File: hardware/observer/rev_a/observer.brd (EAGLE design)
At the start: 44.5 x 44.5 mm, 27 parts, among them J1 CON_HEADER_2X05-PTH+SHROUDED_A, U1 LPS331AP, U2 MPU-9250, U3 SI1147, U4 SI7021, U5 ATUM

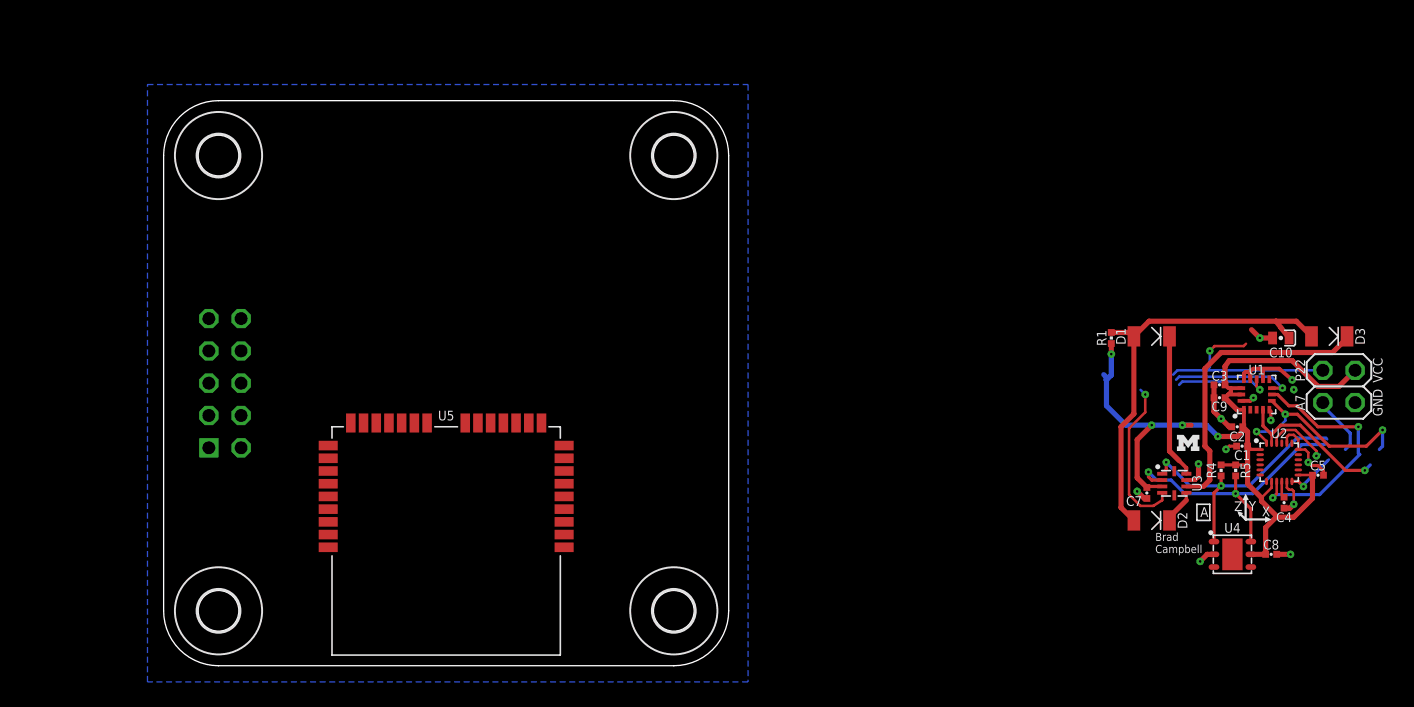
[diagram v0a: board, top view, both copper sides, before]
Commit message: mostly routed
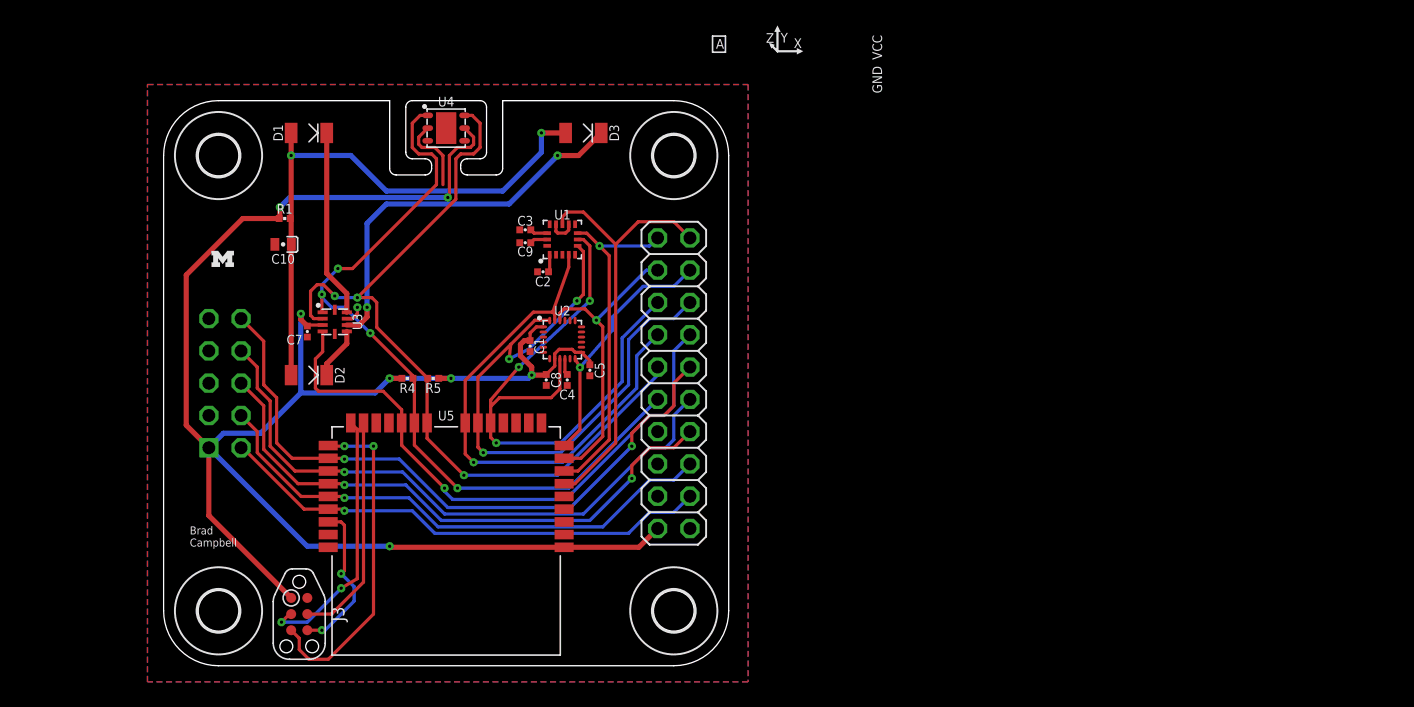
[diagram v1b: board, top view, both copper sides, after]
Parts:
- removed J2: (no value), pinhead:2X02
- added J3: TC2030-CC2538-BL-NL, connector:TC2030-IDC-NL
- added JP1: (no value), pinhead:2X10
- moved C10 78.8 mm to (9.40, 33.1)
- moved LOGO1 77.3 mm to (4.65, 32.0)
- moved U4 70.4 mm to (22.2, 42.3)
- moved D1 68.2 mm to (11.4, 41.9)
- moved D2 67.3 mm to (11.4, 22.9)
- moved C7 67.3 mm to (11.3, 26.3)
- moved U3 67.3 mm to (13.5, 27.1)
- moved R1 65.7 mm to (9.53, 35.2), turned to 180 degrees
- moved R4 64.4 mm to (19.2, 22.6), turned to 180 degrees
- moved R5 63.5 mm to (21.2, 22.6), turned to 0 degrees
- moved D3 60.8 mm to (33.0, 41.9)
- moved C8 58.6 mm to (30.1, 22.5), turned to 270 degrees
- moved C5 57.9 mm to (33.5, 23.2), turned to 270 degrees
- moved C4 57.2 mm to (31.8, 22.5)
- moved U2 57.2 mm to (31.4, 25.7)
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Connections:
- removed net 3V3: J1.1
- removed net A7: J2.2
- removed net MOTOR_CTRL: J2.4
- new net !RESET: J3.6, U5.30
- new net AA: JP1.13
- new net BB: JP1.15
- new net BTLDR_CTRL: J3.5, U5.24
- new net BTLDR_RX: J3.4, U5.22
- new net BTLDR_TX: J3.3, U5.23
- new net CC: JP1.17
- new net UNUSED: U5.21
- new net UNUSED2: U5.20
- net !ACCEL_CS: now also JP1.3, U5.8
- net !BBB_CS: now also JP1.12
- net !PRESSURE_CS: now also JP1.1, U5.7
- net ACCEL_INT: now also JP1.4, U5.9
- net BBB_INT: now also JP1.10
- net BBB_MISO: now also JP1.16
- net BBB_MOSI: now also JP1.18
- net BBB_SCLK: now also JP1.14
- net GND: now also J3.2, JP1.20; no longer J2.1
- net LIGHT_INT: now also JP1.8, U5.19
- net MISO: now also JP1.5
- net MOSI: now also JP1.6
- net PRESSURE_INT: now also JP1.2, U5.6
- net SCL: now also JP1.9
- net SCLK: now also JP1.7
- net SDA: now also JP1.11
- net VCC: now also J1.1, J3.1, JP1.19; no longer J2.3
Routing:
- net VCC: track 69.4 -> 153.4 mm, vias 4 -> 7
- net BBB_INT: track 0.00 -> 51.8 mm, vias 0 -> 2
- net !BBB_CS: track 0.00 -> 48.5 mm, vias 0 -> 1
- net BBB_SCLK: track 0.00 -> 45.3 mm, vias 0 -> 2
- net BBB_MISO: track 0.00 -> 42.0 mm, vias 0 -> 1
- net SCL: track 23.4 -> 64.4 mm, vias 2 -> 3
- net SDA: track 21.5 -> 61.1 mm, vias 2 -> 4
- net BBB_MOSI: track 0.00 -> 39.3 mm, vias 0 -> 1
- net LIGHT_INT: track 12.6 -> 47.5 mm
- net MOSI: track 16.7 -> 49.8 mm
- net SCLK: track 12.6 -> 41.4 mm
- net MISO: track 19.7 -> 47.8 mm, vias 2 -> 3
- net PRESSURE_INT: track 7.64 -> 34.1 mm, vias 1 -> 0
- net BTLDR_CTRL: track 0.00 -> 26.2 mm, vias 0 -> 2
- net BTLDR_TX: track 0.00 -> 20.8 mm, vias 0 -> 2
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- added copper zone on layer 1, net GND
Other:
- outline, holes or cut-outs redrawn
- board text removed: "A7"
- board text removed: "P22"

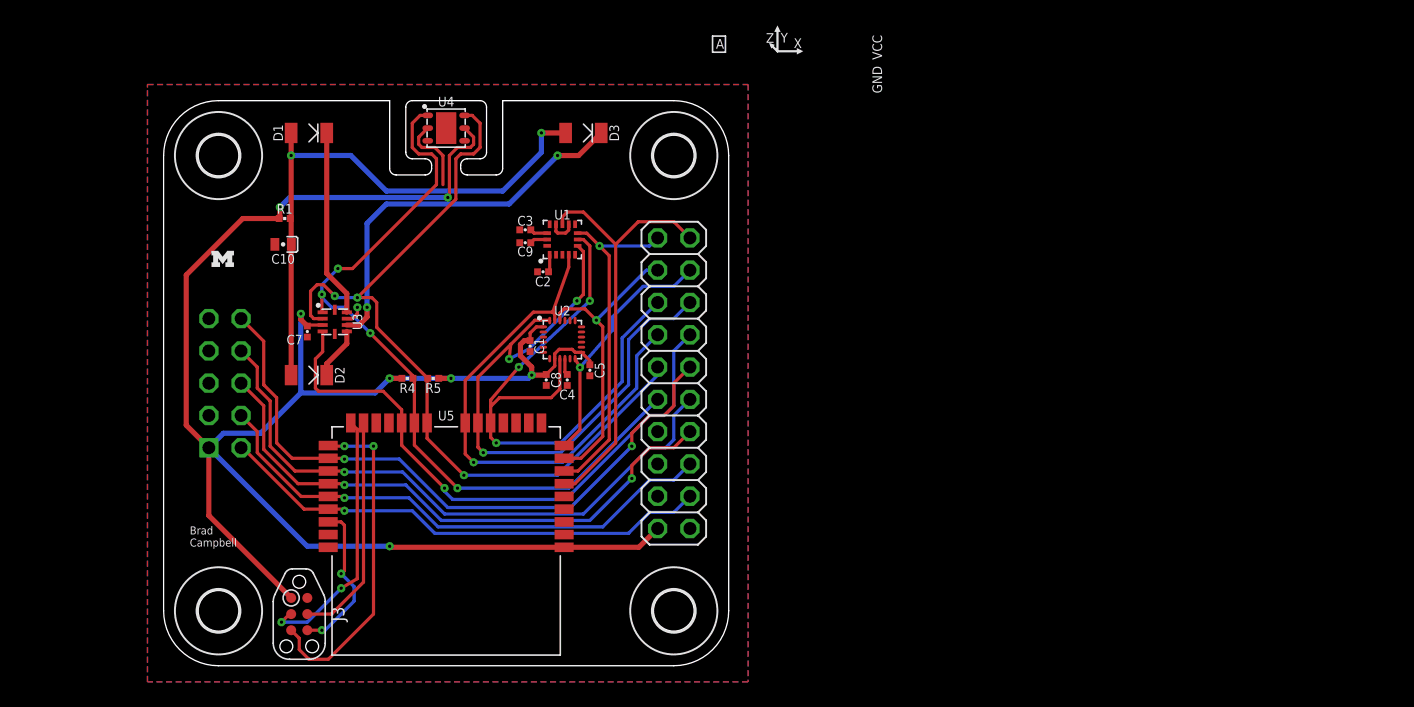
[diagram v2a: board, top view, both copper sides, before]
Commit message: new design with mountable sensor board
If the sensor board doesn't need to be attached elsewhere, it can be
attached to the BBB cape.
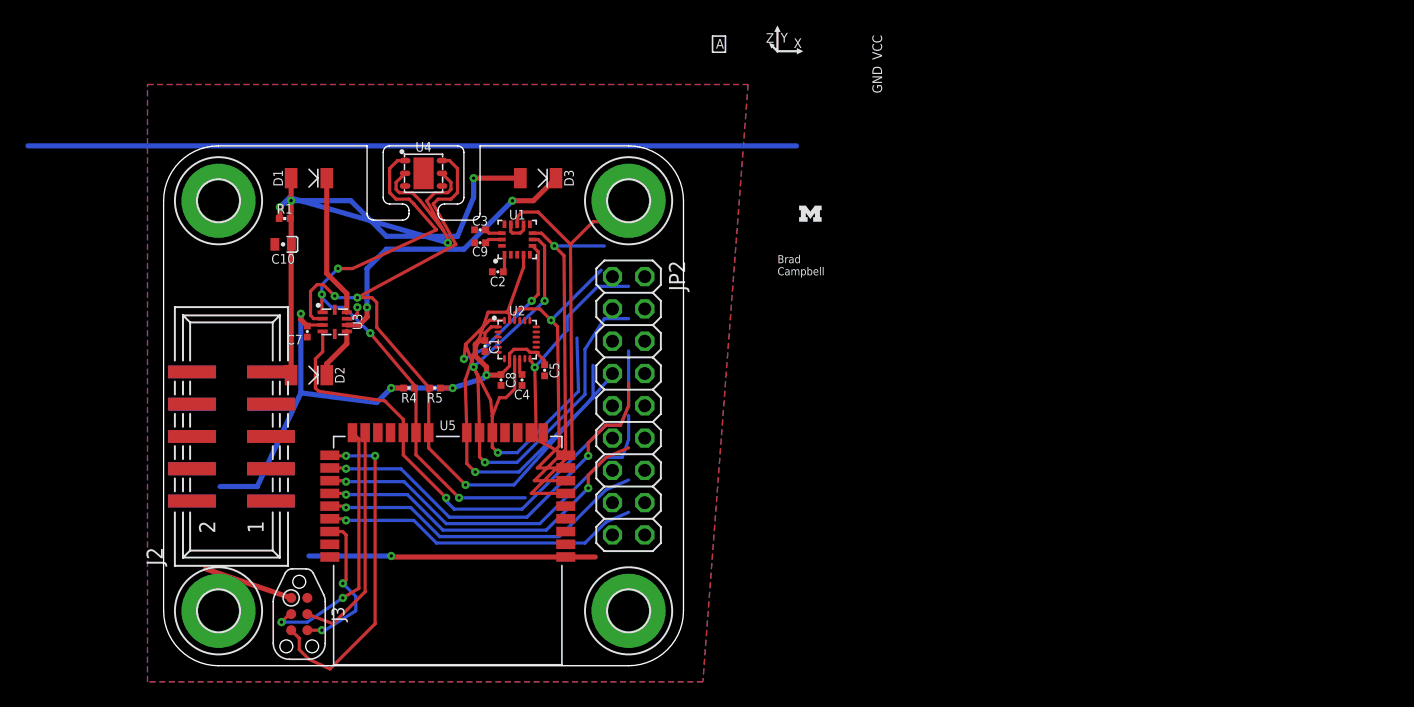
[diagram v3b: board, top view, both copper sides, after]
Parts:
- removed H1, H2, H3, H4: MOUNT-HOLE3.2, holes:3,2
- removed JP1: (no value), pinhead:2X10
- added H5, H6, H7, H8: MOUNT-PAD-ROUND3.2, holes:3,2-PAD
- added J2: CON_HEADER_2X05-SMD+SHROUDED, dp_devices:PINSHRD_SMT_2X05
- added JP2: (no value), pinhead:2X09
- J1: value CON_HEADER_2X05-PTH+SHROUDED_A -> CON_HEADER_2X05-SMD+SHROUDED; device dp_devices:PINSHRD_PTH_2X05 -> dp_devices:PINSHRD_SMT_2X05
- moved LOGO1 46.4 mm to (50.9, 35.6)
- moved D3 5.03 mm to (29.5, 38.4)
- moved J1 4.22 mm to (5.33, 18.0)
- moved U4 3.98 mm to (20.4, 38.7)
- moved C1 3.56 mm to (25.3, 25.1)
- moved C3 3.56 mm to (24.9, 34.3)
- moved C4 3.56 mm to (28.2, 22.5)
- moved C8 3.56 mm to (26.5, 22.5)
- moved C9 3.56 mm to (24.9, 33.3)
- moved U1 3.56 mm to (27.8, 33.5)
- moved U2 3.56 mm to (27.8, 25.7)
- moved C2 3.56 mm to (26.3, 31.0)
- moved C5 3.56 mm to (30.0, 23.2)
- moved D1 3.56 mm to (11.4, 38.4)
- moved R4 0.77 mm to (19.3, 21.8)
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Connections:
- removed net AA: JP1.13
- removed net BB: JP1.15
- removed net BBB_GPIO0: J1.7
- removed net CC: JP1.17
- new net BBB_GPIO: J1.7, J2.7
- new net N$22: JP2.13
- net !ACCEL_CS: now also JP2.3; no longer JP1.3
- net !BBB_CS: now also J2.8, JP2.12; no longer JP1.12
- net !PRESSURE_CS: now also JP2.1; no longer JP1.1
- net 5V: now also J2.3
- net ACCEL_INT: now also JP2.4; no longer JP1.4
- net BBB_INT: now also J2.10, JP2.10; no longer JP1.10
- net BBB_MISO: now also J2.4; no longer JP1.16
- net BBB_MOSI: now also J2.2, JP2.15, JP2.16; no longer JP1.18
- net BBB_SCLK: now also J2.6, JP2.14; no longer JP1.14
- net GND: now also H5.B3,2, H6.B3,2, H7.B3,2, H8.B3,2, J2.9, JP2.18; no longer JP1.20
- net LIGHT_INT: now also JP2.8; no longer JP1.8
- net MISO: now also JP2.5; no longer JP1.5
- net MOSI: now also JP2.6; no longer JP1.6
- net PRESSURE_INT: now also JP2.2; no longer JP1.2
- net SCL: now also JP2.9; no longer JP1.9
- net SCLK: now also JP2.7; no longer JP1.7
- net SDA: now also JP2.11; no longer JP1.11
- net VCC: now also J2.1, JP2.17; no longer JP1.19
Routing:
- net N$1: track 0.00 -> 60.5 mm
- net VCC: track 153.4 -> 105.6 mm
- net BBB_INT: track 51.8 -> 31.5 mm
- net !BBB_CS: track 48.5 -> 29.9 mm
- net BBB_SCLK: track 45.3 -> 27.8 mm
- net BBB_MISO: track 42.0 -> 26.2 mm
- net SDA: track 61.1 -> 46.9 mm
- net BBB_MOSI: track 39.3 -> 25.1 mm
- net MISO: track 47.8 -> 38.3 mm
- net N$7: track 30.6 -> 23.5 mm
- net SCLK: track 41.4 -> 34.4 mm
- net N$8: track 44.6 -> 38.2 mm
- net MOSI: track 49.8 -> 44.9 mm
- net SCL: track 64.4 -> 59.6 mm
- net LIGHT_INT: track 47.5 -> 42.9 mm
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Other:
- board size 44.5 x 44.5 mm -> 40.9 x 40.9 mm

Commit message: working on sensor board
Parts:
- removed JP2: (no value), pinhead:2X09
- added J4: PINHD-2X6/SMD, headers:2X6/SMD
- added U6: AMN41121, chips:AMN2
- moved J1 30.0 mm to (35.3, 18.8), turned to 270 degrees
- moved J2 30.0 mm to (35.3, 18.8), turned to 270 degrees
- moved J3 19.6 mm to (30.2, 4.06), flipped to the bottom
- moved C1 16.9 mm to (11.8, 15.0)
- moved C4 16.9 mm to (14.7, 12.3)
- moved C5 16.9 mm to (16.5, 13.1)
- moved C8 16.9 mm to (13.1, 12.3)
- moved U2 16.9 mm to (14.4, 15.5)
- moved C3 11.5 mm to (27.7, 23.1), turned to 0 degrees
- moved U1 10.1 mm to (24.8, 23.9), turned to 270 degrees
- moved C9 9.56 mm to (27.7, 24.1), turned to 0 degrees
- moved C2 4.57 mm to (26.3, 26.4), turned to 0 degrees
- moved U5 3.81 mm to (18.5, 18.0), flipped to the bottom
- moved C7 3.41 mm to (9.78, 23.2)
- moved U3 3.41 mm to (11.9, 24.0)
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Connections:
- removed net N$22: JP2.13
- removed net UNUSED: U5.21
- removed net UNUSED2: U5.20
- new net PIR_OUT: U5.7, U6.OUT
- new net UN: U5.6
- net !ACCEL_CS: now also J4.8; no longer JP2.3
- net !BBB_CS: now also U5.28; no longer JP2.12, U5.26
- net !PRESSURE_CS: now also J4.1, J4.11, U5.20; no longer JP2.1, U5.7
- net ACCEL_INT: now also J4.4; no longer JP2.4
- net BBB_INT: now also U5.29; no longer JP2.10, U5.25
- net BBB_MISO: now also U5.26; no longer U5.28
- net BBB_MOSI: now also U5.25; no longer JP2.15, JP2.16, U5.29
- net BBB_SCLK: no longer JP2.14
- net GND: now also U6.GND; no longer JP2.18
- net LIGHT_INT: now also J4.9; no longer JP2.8
- net MISO: now also J4.5; no longer JP2.5
- net MOSI: now also J4.6; no longer JP2.6
- net PRESSURE_INT: now also J4.12, J4.2, U5.21; no longer JP2.2, U5.6
- net SCL: now also J4.3; no longer JP2.9
- net SCLK: now also J4.7; no longer JP2.7
- net SDA: now also J4.10; no longer JP2.11
- net VCC: now also U6.VCC; no longer JP2.17
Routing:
- net VCC: track 105.6 -> 12.1 mm, vias 7 -> 1
- net N$1: track 60.5 -> 0.00 mm
- net SCL: track 59.6 -> 7.76 mm, vias 3 -> 0
- net MOSI: track 44.9 -> 0.00 mm, vias 3 -> 0
- net MISO: track 38.3 -> 0.00 mm, vias 3 -> 0
- net N$8: track 38.2 -> 0.00 mm, vias 2 -> 0
- net SCLK: track 34.4 -> 0.00 mm, vias 1 -> 0
- net LIGHT_INT: track 42.9 -> 18.2 mm
- net !ACCEL_CS: track 24.3 -> 0.00 mm, vias 1 -> 0
- net SDA: track 46.9 -> 22.9 mm, vias 4 -> 1
- net N$7: track 23.5 -> 0.00 mm, vias 2 -> 0
- net PRESSURE_INT: track 34.9 -> 14.3 mm, vias 0 -> 1
- net ACCEL_INT: track 19.8 -> 0.00 mm, vias 1 -> 0
- net BBB_INT: track 31.5 -> 12.3 mm, vias 2 -> 1
- net !BBB_CS: track 29.9 -> 13.4 mm
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
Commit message: basically done with observer
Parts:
- removed J4: PINHD-2X6/SMD, headers:2X6/SMD
- added J5: PINHD-2X8/SMD, headers:2X8/SMD
- moved R1 13.3 mm to (8.38, 22.0)
- moved LOGO1 12.9 mm to (38.9, 30.7)
- moved C2 10.7 mm to (25.0, 15.7)
- moved C3 10.7 mm to (26.4, 12.4)
- moved U1 10.7 mm to (23.5, 13.2)
- moved C9 10.7 mm to (26.4, 13.5)
- moved R5 6.72 mm to (19.6, 15.4), turned to 270 degrees
- moved R4 6.63 mm to (20.7, 15.4), turned to 270 degrees
- moved C5 1.53 mm to (18.0, 13.0)
- moved C8 1.48 mm to (14.4, 11.6)
- moved U2 1.48 mm to (15.6, 14.7)
- moved C4 1.17 mm to (15.6, 11.6)
- moved C1 1.17 mm to (12.7, 15.7), turned to 180 degrees
- moved C10 0.90 mm to (9.27, 34.0)
- moved C7 0.79 mm to (9.88, 22.5)
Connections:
- new net N$2: J5.3
- new net N$20: J5.4
- new net UNUSED3: J5.6
- net !ACCEL_CS: now also J5.7, U5.9; no longer J4.8, U5.8
- net !PRESSURE_CS: now also J5.15; no longer J4.1, J4.11
- net ACCEL_INT: now also J5.8, U5.8; no longer J4.4, U5.9
- net GND: now also J5.2
- net LIGHT_INT: now also J5.13; no longer J4.9
- net MISO: now also J5.10; no longer J4.5
- net MOSI: now also J5.9; no longer J4.6
- net PIR_OUT: now also J5.5
- net PRESSURE_INT: now also J5.16; no longer J4.12, J4.2
- net SCL: now also J5.11; no longer J4.3
- net SCLK: now also J5.12; no longer J4.7
- net SDA: now also J5.14; no longer J4.10
- net VCC: now also J5.1
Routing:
- net VCC: track 12.1 -> 152.4 mm, vias 1 -> 8
- net SCL: track 7.76 -> 59.9 mm, vias 0 -> 4
- net N$8: track 0.00 -> 45.5 mm, vias 0 -> 2
- net SDA: track 22.9 -> 52.8 mm, vias 1 -> 5
- net N$7: track 0.00 -> 28.4 mm, vias 0 -> 2
- net MOSI: track 0.00 -> 28.0 mm, vias 0 -> 3
- net SCLK: track 0.00 -> 25.9 mm, vias 0 -> 3
- net PIR_OUT: track 0.00 -> 23.1 mm, vias 0 -> 1
- net MISO: track 0.00 -> 22.9 mm, vias 0 -> 2
- net !ACCEL_CS: track 0.00 -> 22.2 mm, vias 0 -> 2
- net !RESET: track 0.00 -> 17.4 mm
- net ACCEL_INT: track 0.00 -> 17.2 mm, vias 0 -> 1
- net LIGHT_INT: track 18.2 -> 32.7 mm, vias 1 -> 2
- net N$4: track 0.00 -> 13.6 mm
- net GND: track 12.0 -> 19.0 mm, vias 1 -> 20
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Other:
- board text added: "2012/12/16"
- board text added: "Observer"
- board text removed: "GND"
- board text removed: "VCC"

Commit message: slight changes
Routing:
- net GND: vias 20 -> 22
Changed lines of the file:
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@@
 <setting verticaltext="up"/>
 </settings>
-<grid distance="0.005" unitdist="inch" unit="inch" style="lines" multiple="1" display="yes" altdistance="0.005" altunitdist="inch" altunit="inch"/>
+<grid distance="0.05" unitdist="inch" unit="inch" style="lines" multiple="1" display="yes" altdistance="0.005" altunitdist="inch" altunit="inch"/>
 <layers>
 <layer number="1" name="Top" color="4" fill="1" visible="yes" active="yes"/>
@@
 <layer number="14" name="Route14" color="1" fill="6" visible="no" active="no"/>
 <layer number="15" name="Route15" color="4" fill="6" visible="no" active="no"/>
-<layer number="16" name="Bottom" color="1" fill="1" visible="no" active="yes"/>
+<layer number="16" name="Bottom" color="1" fill="1" visible="yes" active="yes"/>
 <layer number="17" name="Pads" color="2" fill="1" visible="yes" active="yes"/>
 <layer number="18" name="Vias" color="2" fill="1" visible="yes" active="yes"/>
@@
 <layer number="20" name="Dimension" color="15" fill="1" visible="yes" active="yes"/>
 <layer number="21" name="tPlace" color="7" fill="1" visible="yes" active="yes"/>
-<layer number="22" name="bPlace" color="7" fill="1" visible="no" active="yes"/>
+<layer number="22" name="bPlace" color="7" fill="1" visible="yes" active="yes"/>
 <layer number="23" name="tOrigins" color="15" fill="1" visible="yes" active="yes"/>
-<layer number="24" name="bOrigins" color="15" fill="1" visible="no" active="yes"/>
+<layer number="24" name="bOrigins" color="15" fill="1" visible="yes" active="yes"/>
 <layer number="25" name="tNames" color="7" fill="1" visible="yes" active="yes"/>
 <layer number="26" name="bNames" color="7" fill="1" visible="no" active="yes"/>
@@
 <rectangle x1="30.861" y1="19.431" x2="32.639" y2="20.574" layer="21"/>
 <rectangle x1="30.861" y1="17.018" x2="32.639" y2="18.161" layer="21"/>
-<wire x1="39.751" y1="20.574" x2="37.973" y2="20.574" width="0.2032" layer="21"/>
-<wire x1="37.973" y1="20.574" x2="37.973" y2="19.558" width="0.2032" layer="21"/>
-<wire x1="39.751" y1="20.574" x2="39.751" y2="19.558" width="0.2032" layer="21"/>
-<wire x1="39.751" y1="18.034" x2="39.751" y2="17.018" width="0.2032" layer="21"/>
-<wire x1="39.751" y1="17.018" x2="37.973" y2="17.018" width="0.2032" layer="21"/>
-<wire x1="37.973" y1="17.018" x2="37.973" y2="18.034" width="0.2032" layer="21"/>
-<rectangle x1="37.973" y1="19.558" x2="39.751" y2="20.574" layer="21"/>
-<rectangle x1="37.973" y1="17.018" x2="39.751" y2="18.034" layer="21"/>
+<wire x1="39.751" y1="20.574" x2="37.973" y2="20.574" width="0.2032" layer="22"/>
+<wire x1="37.973" y1="20.574" x2="37.973" y2="19.558" width="0.2032" layer="22"/>
+<wire x1="39.751" y1="20.574" x2="39.751" y2="19.558" width="0.2032" layer="22"/>
+<wire x1="39.751" y1="18.034" x2="39.751" y2="17.018" width="0.2032" layer="22"/>
+<wire x1="39.751" y1="17.018" x2="37.973" y2="17.018" width="0.2032" layer="22"/>
+<wire x1="37.973" y1="17.018" x2="37.973" y2="18.034" width="0.2032" layer="22"/>
+<rectangle x1="37.973" y1="19.558" x2="39.751" y2="20.574" layer="22"/>
+<rectangle x1="37.973" y1="17.018" x2="39.751" y2="18.034" layer="22"/>
 </plain>
 <attributes>
@@
 <via x="17.272" y="6.096" extent="1-16" drill="0.254"/>
 <via x="11.684" y="6.096" extent="1-16" drill="0.254"/>
+<via x="28.194" y="19.05" extent="1-16" drill="0.254"/>
+<via x="35.941" y="22.225" extent="1-16" drill="0.254"/>
 </signal>
 <signal name="N$3">
@@
 <contactref element="R1" pad="1"/>
 <contactref element="C10" pad="POS"/>
-<wire x1="28.064" y1="38.354" x2="26.67" y2="36.96" width="0.4064" layer="1"/>
-<wire x1="26.67" y1="36.96" x2="26.67" y2="35.306" width="0.4064" layer="1"/>
-<wire x1="26.67" y1="35.306" x2="25.146" y2="33.782" width="0.4064" layer="1"/>
+<wire x1="28.064" y1="36.7" x2="25.146" y2="33.782" width="0.4064" layer="1"/>
 <wire x1="25.146" y1="33.782" x2="22.86" y2="33.782" width="0.4064" layer="1"/>
 <via x="22.86" y="33.782" extent="1-16" drill="0.254"/>
@@
 <wire x1="10.03" y1="38.354" x2="9.921" y2="38.245" width="0.4064" layer="1"/>
 <wire x1="9.921" y1="38.245" x2="9.921" y2="34.036" width="0.4064" layer="1"/>
+<wire x1="28.064" y1="36.7" x2="28.064" y2="38.354" width="0.4064" layer="1"/>
 </signal>
 <signal name="!BBB_CS">
